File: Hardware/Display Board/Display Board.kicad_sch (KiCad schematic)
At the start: 20 parts, among them J1 GPS, J2 RTC, J3 CONT, J4 H:M, J5 M:D, J6 M:S, J7 D:Y

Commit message: Components placed
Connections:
- net MCU RX / GPS TX: now also J1.2 (Pin_2)
- net MCU TX / GPS RX: now also J1.3 (Pin_3)
- net SCL: now also J2.4 (Pin_4)
- net SDA: now also J2.3 (Pin_3)
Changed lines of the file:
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@@
 	)
 	(rectangle
-		(start 46.99 73.66)
+		(start 44.45 73.66)
 		(end 95.25 87.63)
 		(stroke
@@
 	)
 	(rectangle
-		(start 46.99 92.71)
+		(start 44.45 92.71)
 		(end 95.25 106.68)
 		(stroke
@@
 		)
 	)
+	(global_label "SDA"
+		(shape input)
+		(at 52.07 101.6 0)
+		(fields_autoplaced yes)
+		(effects
+			(font
+				(size 1.27 1.27)
+			)
+			(justify left)
+		)
+		(property "Intersheetrefs" "${INTERSHEET_REFS}"
+			(at 58.6233 101.6 0)
+			(effects
+				(font
+					(size 1.27 1.27)
+				)
+				(justify left)
+				(hide yes)
+			)
+		)
+	)
 	(global_label "MCU TX {slash} GPS RX"
 		(shape input)
@@
 		)
 	)
+	(global_label "MCU TX {slash} GPS RX"
+		(shape input)
+		(at 52.07 82.55 0)
+		(fields_autoplaced yes)
+		(effects
+			(font
+				(size 1.27 1.27)
+			)
+			(justify left)
+		)
+		(property "Intersheetrefs" "${INTERSHEET_REFS}"
+			(at 72.7141 82.55 0)
+			(effects
+				(font
+					(size 1.27 1.27)
+				)
+				(justify left)
+				(hide yes)
+			)
+		)
+	)
 	(global_label "SDA"
 		(shape input)
@@
 		)
 	)
+	(global_label "MCU RX {slash} GPS TX"
+		(shape input)
+		(at 52.07 80.01 0)
+		(fields_autoplaced yes)
+		(effects
+			(font
+				(size 1.27 1.27)
+			)
+			(justify left)
+		)
+		(property "Intersheetrefs" "${INTERSHEET_REFS}"
+			(at 72.7141 80.01 0)
+			(effects
+				(font
+					(size 1.27 1.27)
+				)
+				(justify left)
+				(hide yes)
+			)
+		)
+	)
 	(global_label "SDA"
 		(shape input)
@@
 		)
 	)
+	(global_label "SCL"
+		(shape input)
+		(at 52.07 104.14 0)
+		(fields_autoplaced yes)
+		(effects
+			(font
+				(size 1.27 1.27)
+			)
+			(justify left)
+		)
+		(property "Intersheetrefs" "${INTERSHEET_REFS}"
+			(at 58.5628 104.14 0)
+			(effects
+				(font
+					(size 1.27 1.27)
+				)
+				(justify left)
+				(hide yes)
+			)
+		)
+	)
 	(global_label "SDA"
 		(shape input)
@@
 	(symbol
 		(lib_id "power:GND")
-		(at 54.61 96.52 90)
+		(at 52.07 96.52 90)
 		(unit 1)
 		(exclude_from_sim no)
@@
 		(fields_autoplaced yes)
 		(property "Reference" "#PWR015"
-			(at 60.96 96.52 0)
+			(at 58.42 96.52 0)
 			(effects
 				(font
@@
 		)
 		(property "Value" "GND"
-			(at 58.42 96.5199 90)
+			(at 55.88 96.5199 90)
 			(effects
 				(font
@@
 		)
 		(property "Footprint" ""
-			(at 54.61 96.52 0)
+			(at 52.07 96.52 0)
 			(effects
 				(font
@@
 		)
 		(property "Datasheet" ""
-			(at 54.61 96.52 0)
+			(at 52.07 96.52 0)
 			(effects
 				(font
@@
 		)
 		(property "Description" "Power symbol creates a global label with name \"GND\" , ground"
-			(at 54.61 96.52 0)
+			(at 52.07 96.52 0)
 			(effects
 				(font
@@
 	(symbol
 		(lib_id "power:+5V")
-		(at 54.61 85.09 270)
+		(at 52.07 85.09 270)
 		(unit 1)
 		(exclude_from_sim no)
@@
 		(fields_autoplaced yes)
 		(property "Reference" "#PWR014"
-			(at 50.8 85.09 0)
+			(at 48.26 85.09 0)
 			(effects
 				(font
@@
 		)
 		(property "Value" "Vdd"
-			(at 58.42 85.0899 90)
+			(at 55.88 85.0899 90)
 			(effects
 				(font
@@
 		)
 		(property "Footprint" ""
-			(at 54.61 85.09 0)
+			(at 52.07 85.09 0)
 			(effects
 				(font
@@
 		)
 		(property "Datasheet" ""
-			(at 54.61 85.09 0)
+			(at 52.07 85.09 0)
 			(effects
 				(font
@@
 		)
 		(property "Description" "Power symbol creates a global label with name \"+5V\""
-			(at 54.61 85.09 0)
+			(at 52.07 85.09 0)
 			(effects
 				(font
@@
 	(symbol
 		(lib_id "Connector_Generic:Conn_01x04")
-		(at 49.53 99.06 0)
+		(at 46.99 99.06 0)
 		(mirror y)
 		(unit 1)
@@
 		(dnp no)
 		(property "Reference" "J2"
-			(at 49.276 93.726 0)
+			(at 46.736 93.726 0)
 			(effects
 				(font
@@
 		)
 		(property "Value" "RTC"
-			(at 49.53 93.98 0)
+			(at 46.99 93.98 0)
 			(effects
 				(font
@@
 		)
 		(property "Footprint" "Connector_PinSocket_2.54mm:PinSocket_1x04_P2.54mm_Vertical"
-			(at 49.53 99.06 0)
+			(at 46.99 99.06 0)
 			(effects
 				(font
@@
 		)
 		(property "Datasheet" "~"
-			(at 49.53 99.06 0)
+			(at 46.99 99.06 0)
 			(effects
 				(font
@@
 		)
 		(property "Description" "Generic connector, single row, 01x04, script generated (kicad-library-utils/schlib/autogen/connector/)"
-			(at 49.53 99.06 0)
+			(at 46.99 99.06 0)
 			(effects
 				(font
@@
 	(symbol
 		(lib_id "power:GND")
-		(at 54.61 77.47 90)
+		(at 52.07 77.47 90)
 		(unit 1)
 		(exclude_from_sim no)
@@
 		(fields_autoplaced yes)
 		(property "Reference" "#PWR013"
-			(at 60.96 77.47 0)
+			(at 58.42 77.47 0)
 			(effects
 				(font
@@
 		)
 		(property "Value" "GND"
-			(at 58.42 77.4699 90)
+			(at 55.88 77.4699 90)
 			(effects
 				(font
@@
 		)
 		(property "Footprint" ""
-			(at 54.61 77.47 0)
+			(at 52.07 77.47 0)
 			(effects
 				(font
@@
 		)
 		(property "Datasheet" ""
-			(at 54.61 77.47 0)
+			(at 52.07 77.47 0)
 			(effects
 				(font
@@
 		)
 		(property "Description" "Power symbol creates a global label with name \"GND\" , ground"
-			(at 54.61 77.47 0)
+			(at 52.07 77.47 0)
 			(effects
 				(font
@@
 	(symbol
 		(lib_id "Connector_Generic:Conn_01x04")
-		(at 49.53 80.01 0)
+		(at 46.99 80.01 0)
 		(mirror y)
 		(unit 1)
@@
 		(dnp no)
 		(property "Reference" "J1"
-			(at 49.276 74.676 0)
+			(at 46.736 74.676 0)
 			(effects
 				(font
@@
 		)
 		(property "Value" "GPS"
-			(at 49.784 74.93 0)
+			(at 47.244 74.93 0)
 			(effects
 				(font
@@
 		)
 		(property "Footprint" "Connector_PinSocket_2.54mm:PinSocket_1x04_P2.54mm_Vertical"
-			(at 49.53 80.01 0)
+			(at 46.99 80.01 0)
 			(effects
 				(font
@@
 		)
 		(property "Datasheet" "~"
-			(at 49.53 80.01 0)
+			(at 46.99 80.01 0)
 			(effects
 				(font
@@
 		)
 		(property "Description" "Generic connector, single row, 01x04, script generated (kicad-library-utils/schlib/autogen/connector/)"
-			(at 49.53 80.01 0)
+			(at 46.99 80.01 0)
 			(effects
 				(font
@@
 	(symbol
 		(lib_id "power:+5V")
-		(at 54.61 99.06 270)
+		(at 52.07 99.06 270)
 		(unit 1)
 		(exclude_from_sim no)
@@
 		(fields_autoplaced yes)
 		(property "Reference" "#PWR016"
-			(at 50.8 99.06 0)
+			(at 48.26 99.06 0)
 			(effects
 				(font
@@
 		)
 		(property "Value" "Vdd"
-			(at 58.42 99.0599 90)
+			(at 55.88 99.0599 90)
 			(effects
 				(font
@@
 		)
 		(property "Footprint" ""
-			(at 54.61 99.06 0)
+			(at 52.07 99.06 0)
 			(effects
 				(font
@@
 		)
 		(property "Datasheet" ""
-			(at 54.61 99.06 0)
+			(at 52.07 99.06 0)
 			(effects
 				(font
@@
 		)
 		(property "Description" "Power symbol creates a global label with name \"+5V\""
-			(at 54.61 99.06 0)
+			(at 52.07 99.06 0)
 			(effects
 				(font

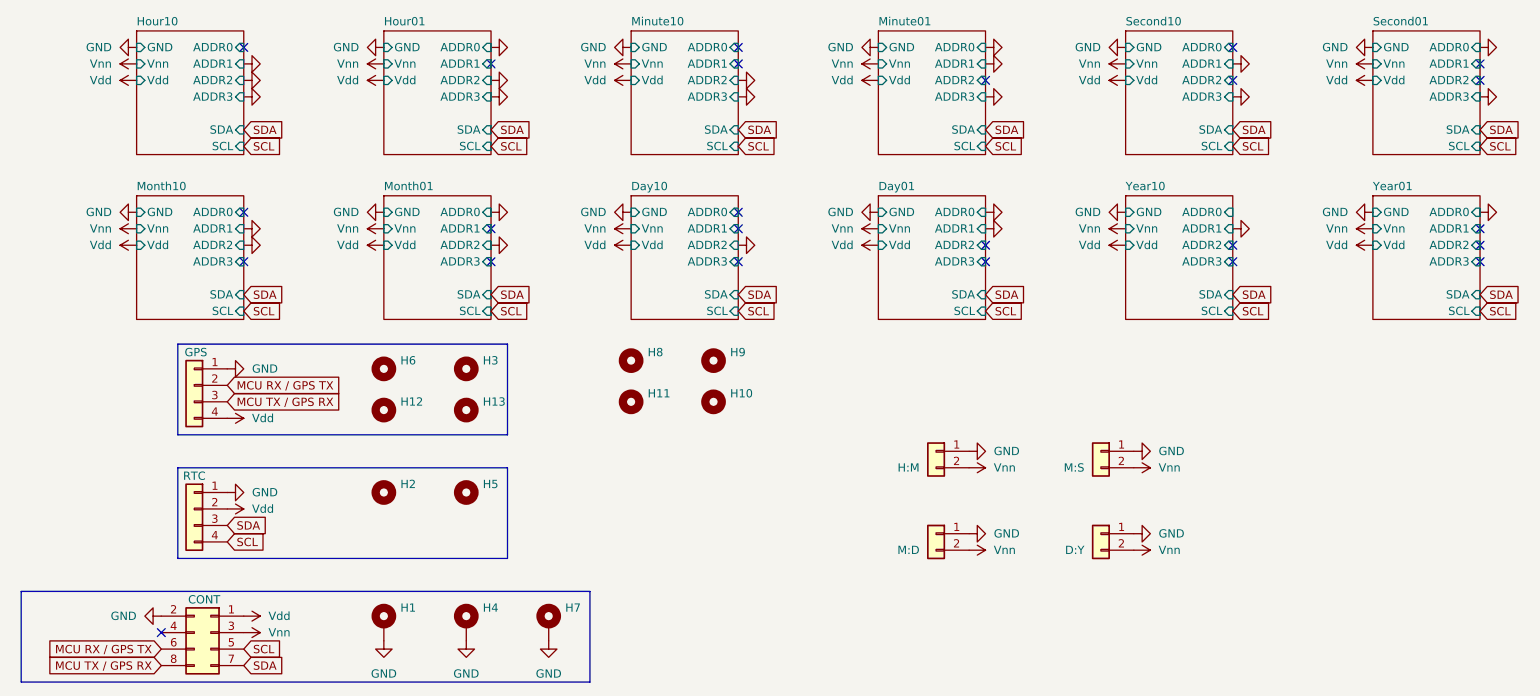
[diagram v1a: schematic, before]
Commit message: KiCad display board completed
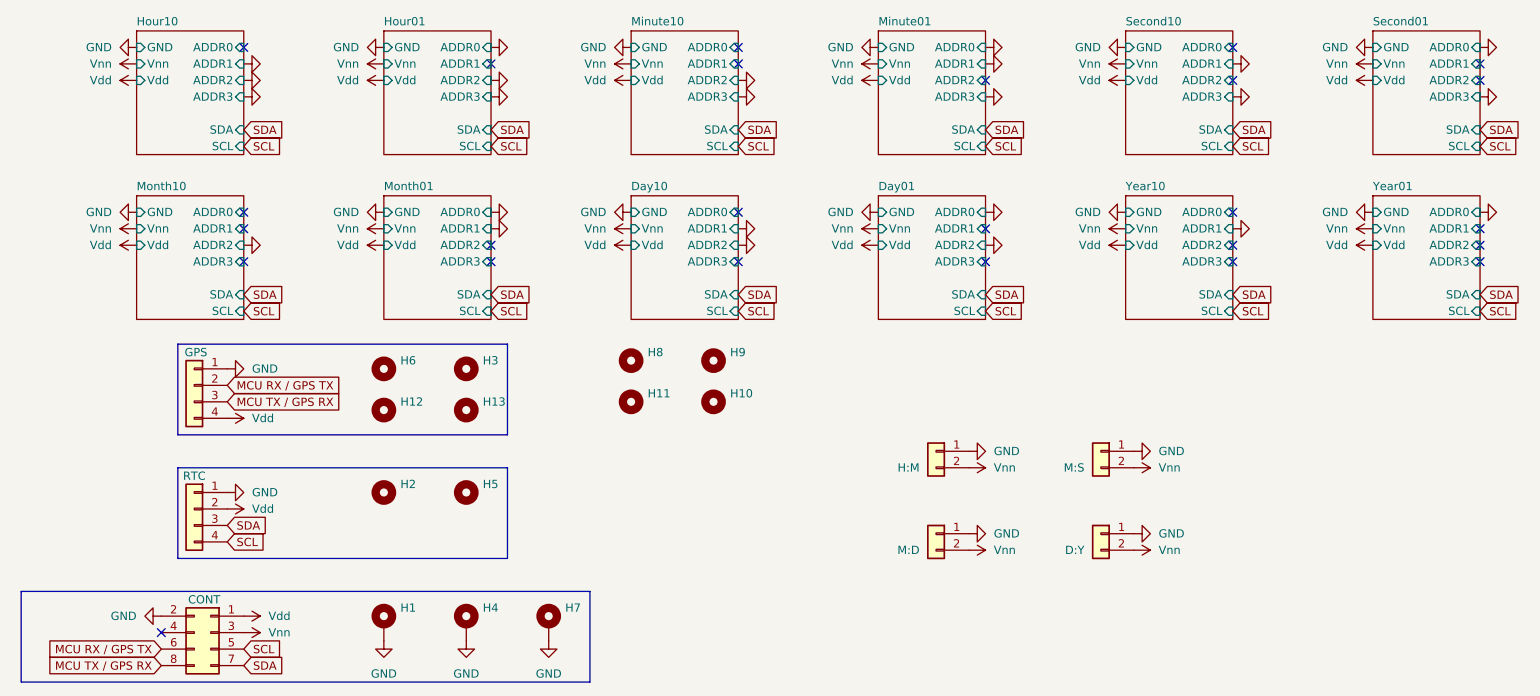
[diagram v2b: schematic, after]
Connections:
- no-connect marks 24 -> 25

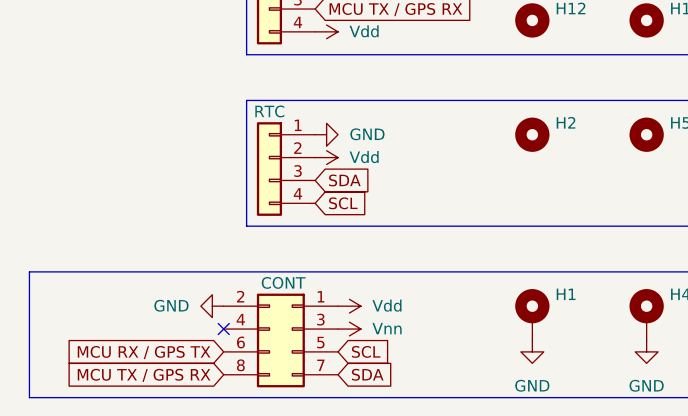
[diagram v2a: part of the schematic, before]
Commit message: Rotated GPS module for better antenna routing
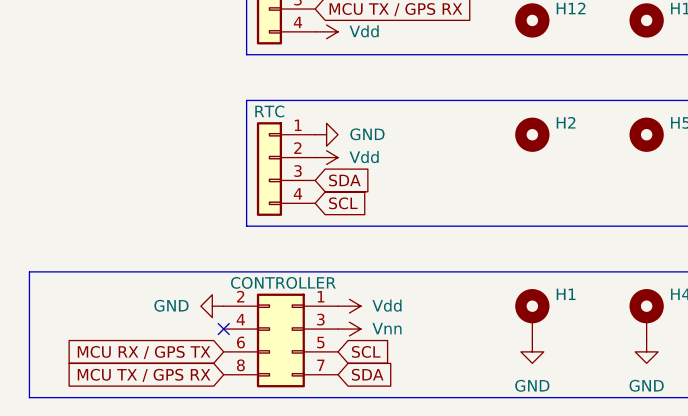
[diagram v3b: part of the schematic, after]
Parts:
- J3: value CONT -> CONTROLLER
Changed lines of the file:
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@@
 			)
 		)
-		(property "Value" "CONT"
+		(property "Value" "CONTROLLER"
 			(at 48.514 113.03 0)
 			(effects

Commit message: Added holes for the antenna holder
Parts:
- added AE1: GPS, DisplayBoard:GPS Antenna Holder, symbol Device:Antenna
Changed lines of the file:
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@@
+	)
+	(symbol
+		(lib_id "Device:Antenna")
+		(at 142.24 78.74 0)
+		(unit 1)
+		(exclude_from_sim no)
+		(in_bom yes)
+		(on_board yes)
+		(dnp no)
+		(fields_autoplaced yes)
+		(property "Reference" "AE1"
+			(at 144.78 78.1049 0)
+			(effects
+				(font
+					(size 1.27 1.27)
+				)
+				(justify left)
+			)
+		)
+		(property "Value" "GPS"
+			(at 144.78 80.6449 0)
+			(effects
+				(font
+					(size 1.27 1.27)
+				)
+				(justify left)
+			)
+		)
+		(property "Footprint" "DisplayBoard:GPS Antenna Holder"
+			(at 142.24 78.74 0)
+			(effects
+				(font
+					(size 1.27 1.27)
+				)
+				(hide yes)
+			)
+		)
+		(property "Datasheet" "~"
+			(at 142.24 78.74 0)
+			(effects
+				(font
+					(size 1.27 1.27)
+				)
+				(hide yes)
+			)
+		)
+		(property "Description" "Antenna"
+			(at 142.24 78.74 0)
+			(effects
+				(font
+					(size 1.27 1.27)
+				)
+				(hide yes)
+			)
+		)
+		(pin "1"
+		)
+		(instances
+			(project ""
+				(path "/599c1f9b-5fc3-4149-97f0-45bd67df2dcb"
+					(reference "AE1")
+					(unit 1)
+				)
+			)
+		)
 	)
 	(symbol

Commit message: Updated Display Board to V2 Nixies
The Antenna holder needs to be redesigned. Lots of silkscreen errors to fix.
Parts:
- removed H12, H13: MountingHole, MountingHole:MountingHole_3.2mm_M3, symbol Mechanical:MountingHole
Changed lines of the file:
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@@
 	)
 	(symbol
-		(lib_id "Mechanical:MountingHole")
-		(at 88.9 83.82 0)
-		(unit 1)
-		(exclude_from_sim yes)
-		(in_bom no)
-		(on_board yes)
-		(dnp no)
-		(fields_autoplaced yes)
-		(property "Reference" "H13"
-			(at 91.44 82.5499 0)
-			(effects
-				(font
-					(size 1.27 1.27)
-				)
-				(justify left)
-			)
-		)
-		(property "Value" "MountingHole"
-			(at 91.44 85.0899 0)
-			(effects
-				(font
-					(size 1.27 1.27)
-				)
-				(justify left)
-				(hide yes)
-			)
-		)
-		(property "Footprint" "MountingHole:MountingHole_3.2mm_M3"
-			(at 88.9 83.82 0)
-			(effects
-				(font
-					(size 1.27 1.27)
-				)
-				(hide yes)
-			)
-		)
-		(property "Datasheet" "~"
-			(at 88.9 83.82 0)
-			(effects
-				(font
-					(size 1.27 1.27)
-				)
-				(hide yes)
-			)
-		)
-		(property "Description" "Mounting Hole without connection"
-			(at 88.9 83.82 0)
-			(effects
-				(font
-					(size 1.27 1.27)
-				)
-				(hide yes)
-			)
-		)
-		(instances
-			(project "Display Board"
-				(path "/599c1f9b-5fc3-4149-97f0-45bd67df2dcb"
-					(reference "H13")
-					(unit 1)
-				)
-			)
-		)
-	)
-	(symbol
 		(lib_id "Mechanical:MountingHole_Pad")
 		(at 88.9 116.84 0)
@@
 					(unit 1)
 				)
-			)
-		)
-	)
-	(symbol
-		(lib_id "Mechanical:MountingHole")
-		(at 76.2 83.82 0)
-		(unit 1)
-		(exclude_from_sim yes)
-		(in_bom no)
-		(on_board yes)
-		(dnp no)
-		(fields_autoplaced yes)
-		(property "Reference" "H12"
-			(at 78.74 82.5499 0)
-			(effects
-				(font
-					(size 1.27 1.27)
-				)
-				(justify left)
-			)
-		)
-		(property "Value" "MountingHole"
-			(at 78.74 85.0899 0)
-			(effects
-				(font
-					(size 1.27 1.27)
-				)
-				(justify left)
-				(hide yes)
-			)
-		)
-		(property "Footprint" "MountingHole:MountingHole_3.2mm_M3"
-			(at 76.2 83.82 0)
-			(effects
-				(font
-					(size 1.27 1.27)
-				)
-				(hide yes)
-			)
-		)
-		(property "Datasheet" "~"
-			(at 76.2 83.82 0)
-			(effects
-				(font
-					(size 1.27 1.27)
-				)
-				(hide yes)
-			)
-		)
-		(property "Description" "Mounting Hole without connection"
-			(at 76.2 83.82 0)
-			(effects
-				(font
-					(size 1.27 1.27)
-				)
-				(hide yes)
-			)
-		)
-		(instances
-			(project "Display Board"
-				(path "/599c1f9b-5fc3-4149-97f0-45bd67df2dcb"
-					(reference "H12")
-					(unit 1)
-				)
